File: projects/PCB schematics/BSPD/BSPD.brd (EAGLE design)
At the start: 160 x 100 mm, 60 parts, among them IC1 LM741D, IC10 74AHC1G32DCK, IC2 LM741D, IC3 OP11D, IC4 OP11D, IC5 OP11D, IC6 OP11D, IC7 74AHC1G32DCK, IC9 NE555D

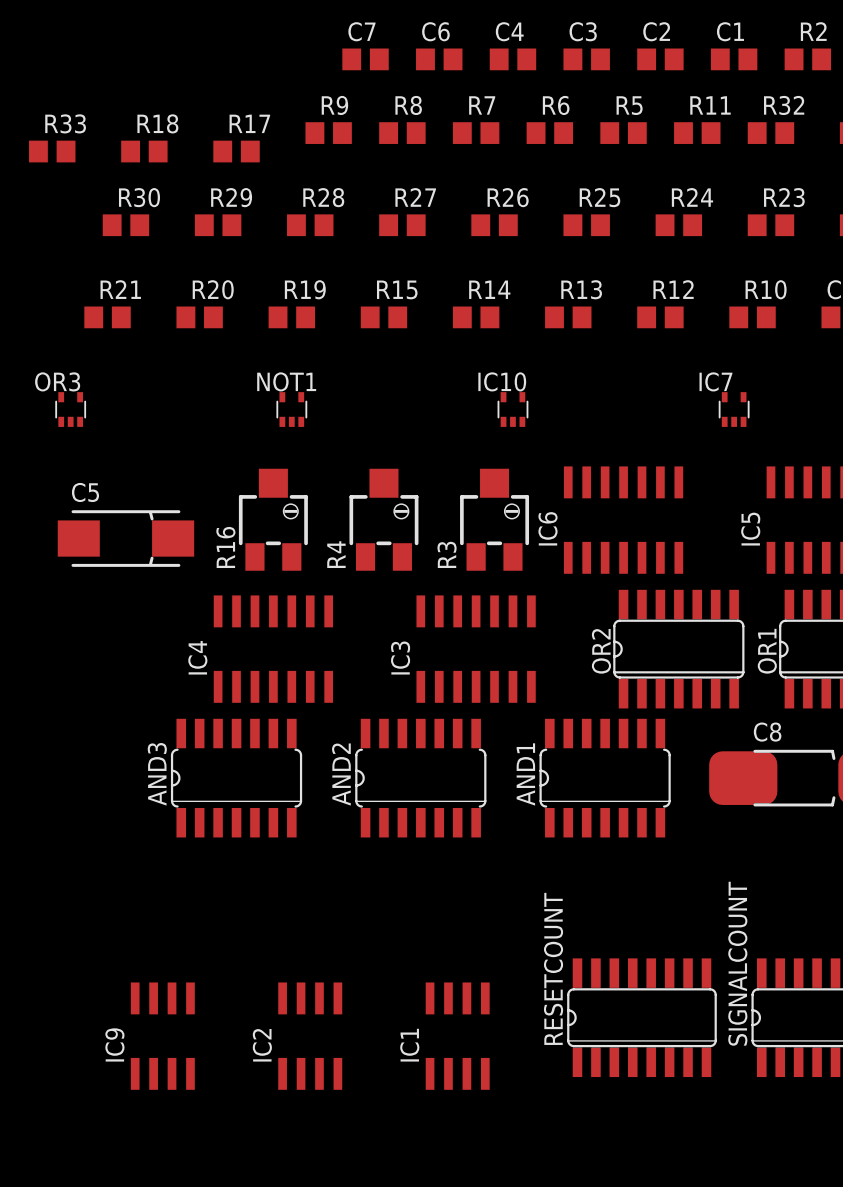
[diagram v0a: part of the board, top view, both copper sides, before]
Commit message: SC - Rev C; SC70 -> SOT23.
For single logic gate components, SC70 was initially chosen.
These packages proved too small to hand-solder.

All SC70 packages have been refactored to SOT23.

SparkFun DRC's added in for additional manufacturability.
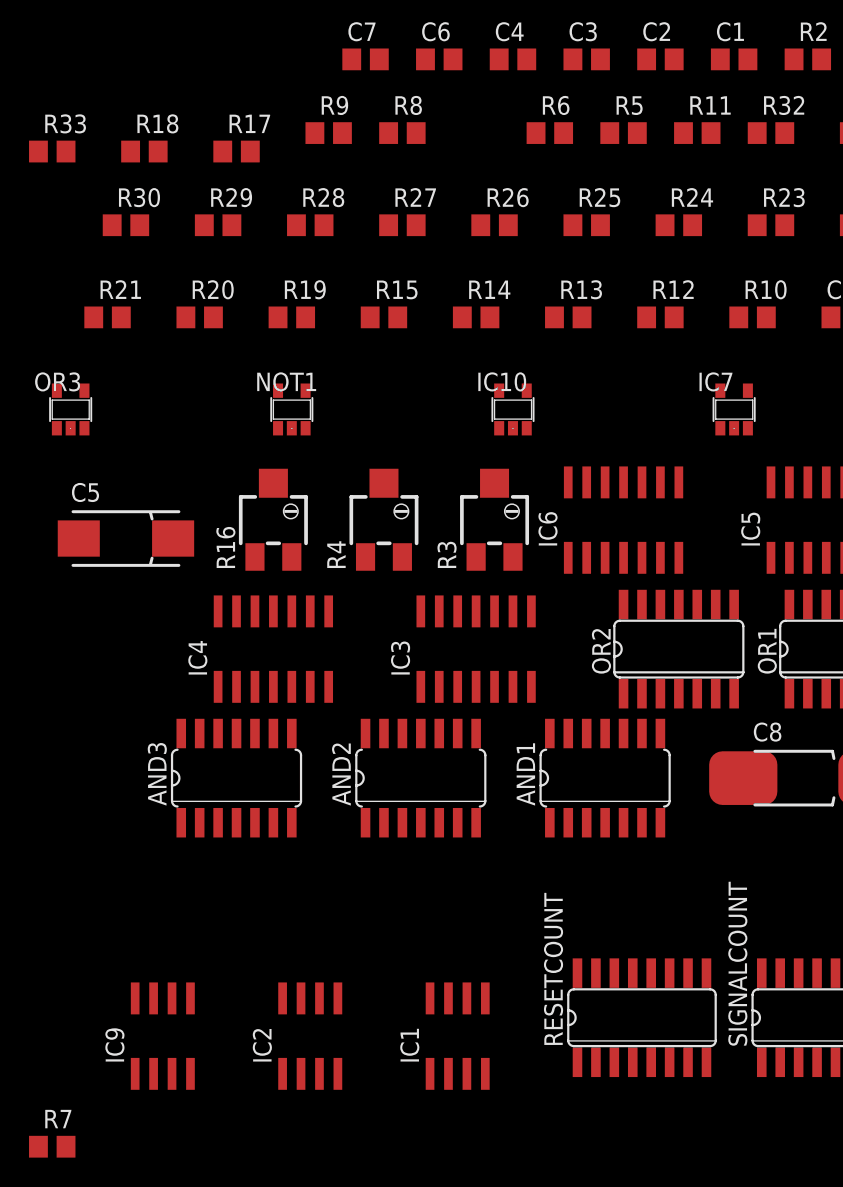
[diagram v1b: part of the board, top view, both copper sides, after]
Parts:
- IC10, IC7, OR3: value 74AHC1G32DCK -> 74AHC1G32DBV; device 74xx-little-de:SC70-5 -> 74xx-little-de:SOT23-5
- NOT1: value 74AHC1G04DCK -> 74AHC1G04DBV; device 74xx-little-us:SC70-5 -> 74xx-little-us:SOT23-5
- R7: value 15k -> (none)
- moved R7 75.7 mm to (-72.4, -3.81)
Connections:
- new net N$61: IC9.7, R33.1, R7.2
- net N$22: no longer R7.1
- net THR: now also R7.1; no longer R33.1, R7.2

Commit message: BSPD - Schematic revision/component revision.
During ESF, schematics chosen used European part libraries.
These were updated to US symbols, with appropriate final parts sourced
to allow builds of both SOP8 and DIL-8 packages.
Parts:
- removed AND1: 74ALS09D, 74xx-eu:SO14
- removed AND2, AND3: 74HC13D, 74xx-eu:SO14
- removed NOT1: 74AHC1G04DBV, 74xx-little-us:SOT23-5
- removed OR1, OR2: 4072D, 40xx:SO14
- removed OR3: 74AHC1G32DBV, 74xx-little-de:SOT23-5
- removed R19: 12k, rcl:R0805
- removed R32: 1k, rcl:R0805
- removed R33: (no value), rcl:R0805
- removed RESETCOUNT, SIGNALCOUNT: 4020D, 40xx:SO16
- added C10, C11, C12, C13, C14, C15: 0.01uF, rcl:C0805
- added IC11: 4020D, 40xx:SO16
- added IC12, IC13: 74LS32D, 74xx-us:SO14
- added IC8: 74ALS09D, 74xx-us:SO14
- added JP1, JP2, JP3, JP4, JP5, JP6, JP7, JP8: (no value), con-lstb:MA03-1
- added RN1, RN2, RN4: (no value), resistor-dil:SOMC16
- added SV1, SV2, SV3, SV4, SV5, SV6: (no value), con-lstb:MA07-2
- added X1: 5566-2, con-molex:5566-2
- C1: device rcl:C0805 -> rcl:085CS_1AR
- C5: device rcl:085CS_1AR -> rcl:C0805
- C8: value 10uF -> 0.01uF; device rcl:085CS_1AW -> rcl:C0805
- C9: value 0.01uF -> 470nF
- IC1, IC2: value LM741D -> OP11D; device linear:SO08 -> linear:SO14
- IC10, IC7: value 74AHC1G32DBV -> 74LS32D; device 74xx-little-de:SOT23-5 -> 74xx-us:SO14
- IC3: value OP11D -> 74LS32D; device linear:SO14 -> 74xx-us:SO14
- IC4: value OP11D -> NE555D; device linear:SO14 -> linear:SO08
- IC5: value OP11D -> 4020D; device linear:SO14 -> 40xx:SO16
- IC9: value NE555D -> 74AHC1G04DBV; device linear:SO08 -> 74xx-little-us:SOT23-5
- R1: value (none) -> 50k
- R11, R12, R5: value 10k -> 50k
- R16: value (none) -> 470; device rcl:RTRIM3224X -> rcl:R0805
- R17: value (none) -> 470
- R18, R2, R7: value (none) -> 10k
- R20, R22: value 27k -> 10k
- R21: value 12k -> 10k
- R23, R24, R25, R26, R27, R28, R29, R30, R31: value 1k -> 10k
- R3, R4: value (none) -> 10k; device rcl:RTRIM3224X -> rcl:R0805
- moved R18 362.7 mm to (31.8, -284.5)
- moved R6 351.2 mm to (31.8, -278.1)
- moved R31 300.0 mm to (-66.0, -229.9)
- moved R30 289.6 mm to (-72.4, -229.9)
- moved R27 283.8 mm to (-66.0, -223.5)
- moved R29 283.3 mm to (-53.3, -223.5)
- moved R28 283.3 mm to (-59.7, -223.5)
- moved R20 277.0 mm to (-72.4, -223.5)
- moved R26 269.7 mm to (-72.4, -208.3)
- moved IC7 266.2 mm to (-67.3, -215.9)
- moved R25 264.2 mm to (-72.4, -201.9)
- moved R24 258.9 mm to (-72.4, -195.6)
- moved R23 253.8 mm to (-72.4, -189.2)
- moved R22 248.9 mm to (-72.4, -182.9)
- moved C9 232.3 mm to (82.5, -156.2), turned to 90 degrees
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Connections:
- removed net BSE: R19.2
- removed net BSE_P: IC1.3, IC3.3, IC3.6, IC4.1
- removed net BSPDFAULT: OR3.4
- removed net MOTCUR: R21.2
- removed net MOTCUR_P: IC2.3, IC5.3, IC5.6, IC6.1
- removed net N$18: IC6.2, R28.1, R29.1
- removed net THR: C8.+, IC9.2, IC9.6, R7.1
- new net BSE_PROCESSED: IC2.3, IC2.6, IC6.3
- new net MOTCUR_PROCESSED: IC1.3, IC1.6, IC6.5
- new net N$62: RN4.7, SV1.3
- new net N$63: RN4.8, SV1.1
- new net N$64: RN4.15, SV2.14
- new net N$65: RN4.14, SV2.12
- new net N$66: RN4.13, SV2.10
- new net N$67: RN4.12, SV2.8
- new net N$68: RN4.11, SV2.6
- new net N$69: RN4.10, SV2.4
- new net N$70: IC5.15, JP8.1
- new net N$71: RN1.2, SV3.13
- new net N$72: RN1.3, SV3.11
- new net N$73: RN1.4, SV3.9
- new net N$74: RN1.5, SV3.7
- new net N$75: RN1.6, SV3.5
- new net N$76: RN1.7, SV3.3
- new net N$77: RN1.8, SV3.1
- new net N$78: RN1.15, SV4.14
- new net N$79: RN1.14, SV4.12
- new net N$80: RN1.13, SV4.10
- new net N$81: RN1.12, SV4.8
- new net N$82: RN1.11, SV4.6
- new net N$83: RN1.10, SV4.4
- new net N$84: RN2.2, SV5.13
- new net N$85: RN2.3, SV5.11
- new net N$86: RN2.4, SV5.9
- new net N$87: RN2.5, SV5.7
- new net N$88: RN2.6, SV5.5
- new net N$89: RN2.7, SV5.3
- new net N$90: RN2.8, SV5.1
- new net N$91: RN2.15, SV6.14
- new net N$92: RN2.14, SV6.12
- new net N$93: RN2.13, SV6.10
- new net N$94: RN2.12, SV6.8
- new net N$95: RN2.11, SV6.6
- new net N$96: RN2.10, SV6.4
- new net N$97: IC5.12, JP2.1
- new net N$98: R18.2
- new net N$99: JP1.3, JP2.3, JP3.3, JP7.3, JP8.3
- new net TR: C9.1, IC4.2, IC4.6, R17.1
- net +0.5V: now also IC1.5, IC2.5, R14.2, R9.1; no longer IC3.5, IC5.5, R14.1, R15.2
- net +1.0V: now also R4.1, R9.2; no longer R13.1, R14.2, R24.2, R29.2
- net +4.0V: now also R13.2, R8.1; no longer R6.1, R8.2
- net +4.5V: now also IC1.2, IC2.2, R2.1, R8.2; no longer IC3.2, IC5.2, R5.1, R6.2
- net +5V: now also C1.+, C2.1, IC4.4, IC4.8, R16.2, R2.2, RN1.1, RN2.1, RN4.1, SV1.10, SV1.12, SV1.14, SV1.2, SV1.4, SV1.6, SV1.8, SV3.10, SV3.12, SV3.14, SV3.2, SV3.4, SV3.6, SV3.8, SV5.10, SV5.12, SV5.14, SV5.2, SV5.4, SV5.6, SV5.8, X1.1; no longer AND3.5, C4.1, C5.+, IC9.4, IC9.8, R16.3, R3.3, R33.2, R4.3, R5.2
- net BSPDPLAUS1: now also IC3.3; no longer IC7.4
- net BSPDPLAUS2: now also IC3.6; no longer IC10.4
- net GND: now also C1.-, C10.2, C11.2, C12.2, C13.2, C14.2, C15.2, C5.2, C8.1, C9.2, IC10.7, IC12.7, IC13.7, IC3.7, IC4.1, IC7.7, IC8.7, IC9.3, JP4.3, JP5.3, JP6.3, R14.1, R18.1, R21.1, R23.1, R24.1, R25.1, R26.1, R27.1, R28.1, R29.1, R30.1, R31.1, R6.1, RN1.9, RN2.9, RN4.9, SV2.1, SV2.11, SV2.13, SV2.2, SV2.3, SV2.5, SV2.7, SV2.9, SV4.1, SV4.11, SV4.13, SV4.2, SV4.3, SV4.5, SV4.7, SV4.9, SV6.1, SV6.11, SV6.13, SV6.2, SV6.3, SV6.5, SV6.7, SV6.9, X1.2; no longer AND1.7, AND2.7, AND3.7, C1.2, C5.-, C8.-, C9.1, IC10.3, IC7.3, IC9.1, NOT1.3, OR2.5, OR3.3, R15.1, R16.1, R25.2, R27.2, R3.1, R30.2, R32.2, R4.1
- net N$1: now also R13.1, R15.2; no longer IC3.1, R1.1
- net N$10: now also C7.1, IC2.12, R12.2; no longer C2.1, IC3.10, R1.2
- net N$11: now also IC1.1, R1.1; no longer C1.1, IC3.12, R2.2
- net N$12: now also C4.1, IC1.10, R1.2; no longer C6.1, IC5.10, R17.2
- net N$13: now also C6.1, IC1.12, R11.2; no longer C7.1, IC5.12, R18.2
- net N$14: now also IC1.7, R11.1; no longer IC5.7, R18.1
- net N$15: now also IC3.10; no longer IC6.3, R30.1, R31.2
- net N$16: now also RN4.2, SV1.13; no longer R21.1, R22.2, R28.2
- net N$17: now also IC13.8, IC3.13; no longer R31.1, R32.1
- net N$19: now also C10.1, C11.1, IC6.2, RN4.16; no longer IC1.2, R3.2
- net N$2: now also R10.2, R15.1; no longer R8.1, R9.2
- net N$20: now also IC7.9, JP1.2; no longer R19.1, R23.2
- net N$21: now also C12.1, C13.1, IC6.6, RN1.16; no longer IC2.2, R4.2
- net N$22: now also IC4.3, IC8.10, IC8.4; no longer AND1.10, AND1.4, IC9.3
- net N$23: now also IC13.6, IC3.12; no longer R26.1, R27.1
- net N$24: now also IC10.9, JP4.2, R21.2; no longer IC4.2, R23.1, R24.1
- net N$25: now also C8.2, IC4.5; no longer C9.2, IC9.5
- net N$26: now also IC6.7, IC8.2; no longer AND1.2, IC2.6
- net N$27: now also IC6.1, IC8.1; no longer AND1.1, IC1.6
- net N$28: now also IC11.11, IC8.3, IC8.5, IC9.2; no longer AND1.3, AND1.5, NOT1.2, RESETCOUNT.11
- net N$29: now also IC8.9, IC9.4; no longer AND1.9, NOT1.4
- net N$3: now also IC3.9, IC5.3, R6.2; no longer IC4.3, R25.1, R26.2
- net N$30: now also IC11.10, IC8.8; no longer AND1.8, RESETCOUNT.10
- net N$31: now also IC11.14, JP5.1; no longer OR1.2, RESETCOUNT.4
- net N$32: now also IC11.12, JP4.1; no longer OR1.3, RESETCOUNT.6
- net N$33: now also IC10.10, JP5.2, R22.2; no longer OR1.4, RESETCOUNT.13
- net N$34: now also IC10.8, IC12.4; no longer OR1.5, RESETCOUNT.12
- net N$35: now also IC10.11, IC12.5; no longer OR1.9, RESETCOUNT.14
- net N$36: now also IC12.10, IC12.3; no longer OR1.10, RESETCOUNT.15
- net N$37: now also IC10.12, JP6.2, R23.2; no longer OR1.11, RESETCOUNT.1
- net N$38: now also IC11.15, JP6.1; no longer OR1.12, RESETCOUNT.2
- net N$39: now also IC12.6, IC12.9; no longer OR1.1, OR2.2
- net N$4: now also R3.2, R7.1; no longer R10.2, R9.1
- net N$40: now also IC5.13, JP1.1; no longer OR1.13, OR2.3
- net N$41: now also IC7.10, JP2.2, R27.2; no longer OR2.4, RESETCOUNT.3
- net N$42: now also IC12.8, IC5.11; no longer OR2.1, SIGNALCOUNT.11
- net N$43: now also IC5.10, IC8.6; no longer AND1.6, SIGNALCOUNT.10
- net N$44: now also IC2.8, IC3.1; no longer IC3.8, IC7.1
- net N$45: now also IC2.14, IC3.2; no longer IC3.14, IC7.2
- net N$46: now also IC1.8, IC3.4; no longer IC10.1, IC5.8
- net N$47: now also IC1.14, IC3.5; no longer IC10.2, IC5.14
- net N$48: now also IC7.12, JP3.2, R28.2; no longer AND2.6, AND3.1
- net N$49: now also IC5.14, JP3.1; no longer AND2.8, AND3.2
- net N$5: now also R3.1, R4.2; no longer R11.1, R12.2
- net N$50: now also IC7.13, JP8.2, R29.2; no longer AND2.13, SIGNALCOUNT.1
- net N$51: now also IC13.1, IC5.1, R30.2; no longer AND2.12, SIGNALCOUNT.15
- net N$52: now also IC10.13, IC11.1, R24.2; no longer AND2.10, SIGNALCOUNT.14
- net N$53: now also IC11.2, IC12.1, R25.2; no longer AND2.9, SIGNALCOUNT.12
- net N$54: now also IC11.3, IC12.2, R26.2; no longer AND2.5, SIGNALCOUNT.13
- net N$55: now also IC13.2, IC5.2, R31.2; no longer AND2.4, SIGNALCOUNT.6
- net N$56: now also IC7.11; no longer AND2.2, SIGNALCOUNT.4
- net N$57: now also RN4.3, SV1.11; no longer AND2.1, SIGNALCOUNT.5
- net N$58: now also RN4.4, SV1.9; no longer AND3.4, SIGNALCOUNT.2
- net N$59: now also RN4.5, SV1.7; no longer OR3.2, SIGNALCOUNT.3
- net N$6: now also R10.1, R7.2; no longer IC5.1, R17.1
- net N$60: now also RN4.6, SV1.5; no longer AND3.6, OR3.1
- net N$61: now also IC4.7, R16.1, R17.2; no longer IC9.7, R33.1, R7.2
- net N$7: now also IC2.1, R5.1; no longer R12.1, R13.2
- net N$8: now also IC2.7, R12.1; no longer IC3.7, R2.1
- net N$9: now also C5.1, IC2.10, R5.2; no longer R10.1, R11.2
- net TIME_THRESH: now also C14.1, C15.1, IC1.13, IC1.9, IC2.13, IC2.9, RN2.16; no longer IC3.13, IC3.9, IC5.13, IC5.9, R16.2
- net V+: now also IC1.4, IC2.4; no longer IC1.7, IC2.7, IC3.4, IC4.4, IC5.4
- net V-: now also IC1.11, IC2.11; no longer IC1.4, IC2.4, IC3.11, IC4.11, IC5.11
- net VCC: now also IC10.14, IC12.14, IC13.14, IC3.14, IC7.14, IC8.14, IC9.5; no longer AND1.14, AND2.14, AND3.14, IC10.5, IC7.5, NOT1.5, OR3.5
- net VDD: now also IC11.16, IC5.16; no longer OR1.14, OR2.14, RESETCOUNT.16, SIGNALCOUNT.16
- net VSS: now also IC11.8, IC5.8; no longer OR1.7, OR2.7, RESETCOUNT.8, SIGNALCOUNT.8
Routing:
- net N$30: track 0.00 -> 57.5 mm
- net VSS: track 0.00 -> 25.8 mm

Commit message: TSALC - Initial build.
Initial build done by Anshuman. 
TSALC is still WIP.
TSALC work must be continued on another branch.
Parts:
- moved JP7 410.7 mm to (133.6, 65.4)
- moved JP2 388.8 mm to (133.6, 94.6)
- moved JP1 381.9 mm to (133.6, 99.7)
- moved JP3 379.2 mm to (133.6, 89.5)
- moved C12 354.6 mm to (198.3, 83.2)
- moved C13 354.6 mm to (206.0, 83.2)
- moved R18 354.6 mm to (198.3, 28.6)
- moved R6 354.6 mm to (198.3, 34.9)
- moved C14 354.6 mm to (198.3, 41.3)
- moved C15 354.6 mm to (206.0, 41.3)
- moved R21 331.4 mm to (106.9, 102.2)
- moved R22 331.4 mm to (106.9, 95.9)
- moved R23 331.4 mm to (106.9, 89.5)
- moved R24 331.4 mm to (106.9, 83.2)
- moved R25 331.4 mm to (106.9, 76.8)
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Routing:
- net GND: track 0.00 -> 730.2 mm, vias 0 -> 9
- net +5V: track 0.00 -> 411.6 mm, vias 0 -> 5
- net TIME_THRESH: track 0.00 -> 302.5 mm, vias 0 -> 4
- net N$21: track 0.00 -> 240.5 mm, vias 0 -> 4
- net N$3: track 0.00 -> 221.5 mm, vias 0 -> 3
- net N$19: track 0.00 -> 211.1 mm, vias 0 -> 5
- net N$51: track 0.00 -> 211.1 mm, vias 0 -> 4
- net +4.5V: track 0.00 -> 188.0 mm, vias 0 -> 3
- net N$55: track 0.00 -> 186.4 mm, vias 0 -> 5
- net N$20: track 0.00 -> 163.6 mm, vias 0 -> 4
- net +0.5V: track 0.00 -> 162.9 mm, vias 0 -> 7
- net N$33: track 0.00 -> 161.9 mm, vias 0 -> 3
- net N$41: track 0.00 -> 161.4 mm, vias 0 -> 3
- net N$50: track 0.00 -> 154.1 mm, vias 0 -> 4
- net N$48: track 0.00 -> 151.3 mm, vias 0 -> 5
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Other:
- board size 160 x 100 mm -> 254 x 111.4 mm
- board text added: "Brake System Plausibility Device(BSPD): Rev A. Date: 28th March 2019"
- board text added: "Iowa Formula"

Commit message: BSPD - Schematic finalized.
BSPD schematic needed final refactoring for parts.
Adjustable threshold settings have been put in for plausibility checks
using resistor arrays.

Squashed - BSPD - Removed BSPD.brd.

Too much work will be required to refactor this board.
It's currently 10 inches long.
Given the work entailed, I'm scrapping the board and relaying from a clean slate.

Squashed - BSPD - Created BSPD.brd.

Board file created.
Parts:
- removed IC13: 74LS32D, 74xx-us:SO14
- added JP10, JP9: (no value), con-lstb:MA03-1
- added R19: 10k, rcl:R0805
- added R32, R33, R34: 50k, rcl:R0805
- added X2: 5566-2, con-molex:5566-2
- added X3: 5566-4, con-molex:5566-4
- IC10: value 74LS32D -> 4020D; device 74xx-us:SO14 -> 40xx:SO16
- IC11: value 4020D -> 74LS32D; device 40xx:SO16 -> 74xx-us:SO14
- R26: value 10k -> 50k
- moved R6 284.5 mm to (-83.8, 71.1)
- moved SV4 266.5 mm to (-80.0, 21.6), turned to 0 degrees
- moved RN4 265.1 mm to (-81.3, 6.35)
- moved C15 247.2 mm to (-40.6, 58.4)
- moved RN2 243.6 mm to (-71.1, 6.35)
- moved SV2 242.5 mm to (-41.9, 21.6), turned to 0 degrees
- moved RN1 237.5 mm to (-61.0, 6.35)
- moved C13 232.7 mm to (-25.4, 58.4)
- moved C14 232.0 mm to (-33.0, 58.4)
- moved SV6 228.9 mm to (-41.9, 31.8), turned to 0 degrees
- moved R18 224.2 mm to (-22.9, 64.8)
- moved SV3 221.1 mm to (-61.0, 21.6), turned to 0 degrees
- moved C12 217.5 mm to (-17.8, 58.4)
- moved C10 216.1 mm to (-78.7, 49.5), turned to 0 degrees
- moved C11 213.6 mm to (-86.4, 49.5), turned to 0 degrees
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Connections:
- removed net N$24: IC10.9, JP4.2, R21.2
- removed net N$28: IC11.11, IC8.3, IC8.5, IC9.2
- removed net N$30: IC11.10, IC8.8
- new net BSPDFAULT: IC7.11, X3.3
- new net N$100: IC5.1, JP7.1
- new net N$101: IC10.1, JP10.1
- new net N$102: IC11.13, IC11.8
- new net N$103: IC11.3, IC12.1
- new net N$104: IC11.6, IC12.2
- new net N$105: IC11.11, IC12.5
- new net N$18: IC3.8, IC7.9
- new net RESET_FAULTCOUNT: IC12.6, IC5.11
- net +5V: now also R26.2, R33.2
- net BSE_PROCESSED: now also R26.1, R32.2, X2.1
- net BSPDPLAUS1: now also X3.1
- net BSPDPLAUS2: now also X3.2
- net GND: now also IC11.7, R19.1, R32.1, R34.1; no longer IC10.7, IC13.7, JP4.3, JP5.3, JP6.3, R26.1
- net MOTCUR_PROCESSED: now also R33.1, R34.2, X2.2
- net N$15: now also IC7.3, IC7.5; no longer IC3.10
- net N$17: now also IC10.11, IC8.3, IC8.5, IC9.2; no longer IC13.8, IC3.13
- net N$20: now also IC3.9; no longer IC7.9
- net N$23: now also IC7.12, IC7.8; no longer IC13.6, IC3.12
- net N$3: now also IC7.4; no longer IC3.9
- net N$31: now also IC11.1, JP4.2, R18.2; no longer IC11.14, JP5.1
- net N$32: now also IC10.13; no longer IC11.12
- net N$33: now also IC11.2, R19.2; no longer IC10.10, R22.2
- net N$34: now also IC11.4, JP6.2, R21.2; no longer IC10.8, IC12.4
- net N$35: now also IC10.14, JP6.1; no longer IC10.11, IC12.5
- net N$36: now also IC11.5, JP9.2, R22.2; no longer IC12.10, IC12.3
- net N$37: now also IC11.9, JP10.2; no longer IC10.12, JP6.2
- net N$38: now also IC10.2, IC11.10, R24.2; no longer IC11.15, JP6.1
- net N$39: now also IC10.12, JP5.1; no longer IC12.6, IC12.9
- net N$41: now also IC3.10; no longer IC7.10
- net N$42: now also IC10.10, IC8.8; no longer IC12.8, IC5.11
- net N$48: now also IC3.12; no longer IC7.12
- net N$50: now also IC3.13; no longer IC7.13
- net N$51: now also IC7.1, JP7.2; no longer IC13.1, IC5.1
- net N$52: now also IC10.15, JP9.1; no longer IC10.13, IC11.1, R24.2
- net N$53: now also IC12.3, IC12.4; no longer IC11.2, IC12.1, R25.2
- net N$54: now also IC10.3, IC11.12, R25.2; no longer IC11.3, IC12.2, R26.2
- net N$55: now also IC7.2; no longer IC13.2
- net N$56: now also IC3.11, IC7.10; no longer IC7.11
- net N$98: now also IC7.13, IC7.6; no longer R18.2
- net N$99: now also JP10.3, JP4.3, JP5.3, JP6.3, JP9.3
- net VCC: now also IC11.14; no longer IC10.14, IC13.14
- net VDD: now also IC10.16; no longer IC11.16
- net VSS: now also IC10.8; no longer IC11.8
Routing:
- net GND: track 730.2 -> 0.00 mm, vias 9 -> 0
- net +5V: track 411.6 -> 0.00 mm, vias 5 -> 0
- net TIME_THRESH: track 302.5 -> 0.00 mm, vias 4 -> 0
- net N$21: track 240.5 -> 0.00 mm, vias 4 -> 0
- net N$3: track 221.5 -> 0.00 mm, vias 3 -> 0
- net N$19: track 211.1 -> 0.00 mm, vias 5 -> 0
- net N$51: track 211.1 -> 0.00 mm, vias 4 -> 0
- net +4.5V: track 188.0 -> 0.00 mm, vias 3 -> 0
- net N$55: track 186.4 -> 0.00 mm, vias 5 -> 0
- net N$20: track 163.6 -> 0.00 mm, vias 4 -> 0
- net +0.5V: track 162.9 -> 0.00 mm, vias 7 -> 0
- net N$33: track 161.9 -> 0.00 mm, vias 3 -> 0
- net N$41: track 161.4 -> 0.00 mm, vias 3 -> 0
- net N$50: track 154.1 -> 0.00 mm, vias 4 -> 0
- net N$48: track 151.3 -> 0.00 mm, vias 5 -> 0
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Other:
- board size 254 x 111.4 mm -> 160 x 100 mm
- board text removed: "Brake System Plausibility Device(BSPD): Rev A. Date: 28th March 2019"
- board text removed: "Iowa Formula"
